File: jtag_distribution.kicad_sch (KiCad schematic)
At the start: 28 parts, among them J16 Conn_ARM_JTAG_SWD_20, SW1 SW_DIP_x04, U2 AMS1117-3.3

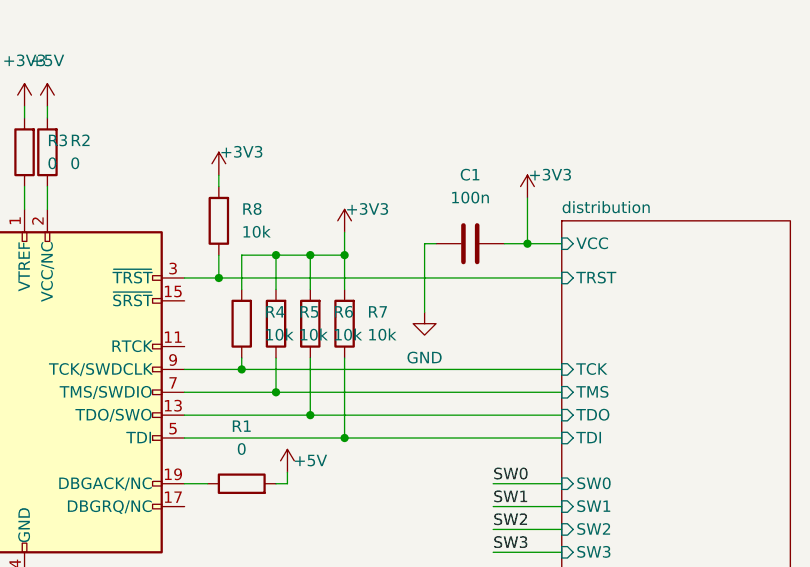
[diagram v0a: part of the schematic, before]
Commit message: change dip switch type, change reset position
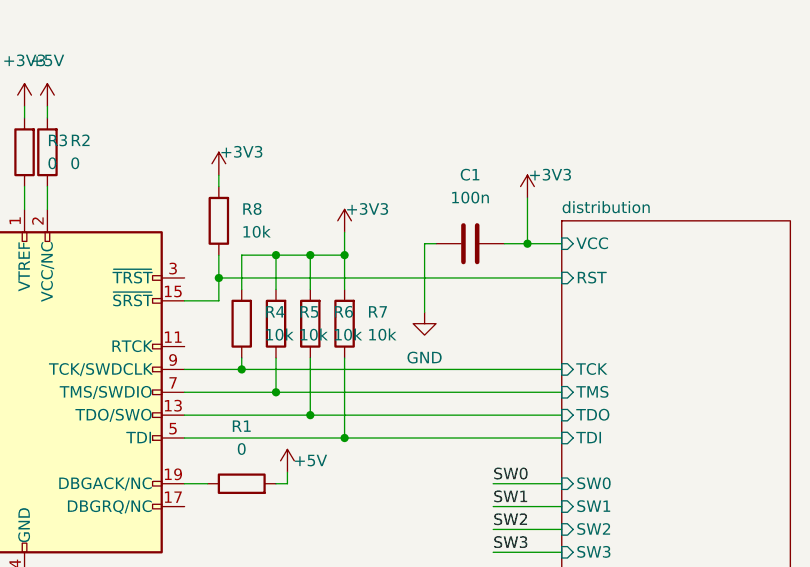
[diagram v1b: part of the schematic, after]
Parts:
- SW1: footprint Button_Switch_SMD:SW_DIP_SPSTx04_Slide_6.7x11.72mm_W8.61mm_P2.54mm_LowProfile -> Button_Switch_THT:SW_DIP_SPSTx04_Slide_6.7x11.72mm_W7.62mm_P2.54mm_LowProfile
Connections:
- net distribution/RST: now reaches J16.15 (~{SRST})
- net distribution/RST: now also R8.1
- net distribution/TRST: no longer names the net of J16.3 (~{TRST})
- net distribution/TRST: no longer R8.1
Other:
- sheet distribution ports: added RST; removed TRST
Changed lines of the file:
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@@
   (junction (at 67.31 157.48) (diameter 0) (color 0 0 0 0)
   )
+  (junction (at 130.81 85.09) (diameter 0) (color 0 0 0 0)
+  )
   (junction (at 212.09 36.83) (diameter 0) (color 0 0 0 0)
   )
@@
   (junction (at 144.78 102.87) (diameter 0) (color 0 0 0 0)
   )
-  (junction (at 130.81 85.09) (diameter 0) (color 0 0 0 0)
-  )
   (junction (at 64.77 154.94) (diameter 0) (color 0 0 0 0)
   )
@@
     (stroke (width 0) (type default))
   )
+  (wire (pts (xy 130.81 85.09) (xy 130.81 87.63))
+    (stroke (width 0) (type default))
+  )
   (wire (pts (xy 137.16 82.55) (xy 137.16 86.36))
     (stroke (width 0) (type default))
@@
     (stroke (width 0) (type default))
   )
-  (wire (pts (xy 127 85.09) (xy 130.81 85.09))
-    (stroke (width 0) (type default))
-  )
   (wire (pts (xy 130.81 85.09) (xy 168.91 85.09))
     (stroke (width 0) (type default))
@@
   )
   (wire (pts (xy 90.17 157.48) (xy 90.17 154.94))
+    (stroke (width 0) (type default))
+  )
+  (wire (pts (xy 127 87.63) (xy 130.81 87.63))
     (stroke (width 0) (type default))
   )
@@
       (effects (font (size 1.27 1.27)))
     )
-    (property "Footprint" "Button_Switch_SMD:SW_DIP_SPSTx04_Slide_6.7x11.72mm_W8.61mm_P2.54mm_LowProfile" (at 80.01 157.48 0)
+    (property "Footprint" "Button_Switch_THT:SW_DIP_SPSTx04_Slide_6.7x11.72mm_W7.62mm_P2.54mm_LowProfile" (at 80.01 157.48 0)
       (effects (font (size 1.27 1.27)) hide)
     )
@@
       (effects (font (size 1.27 1.27)) (justify left))
     )
-    (pin "TRST" input (at 168.91 85.09 180)
-      (effects (font (size 1.27 1.27)) (justify left))
-    )
     (pin "TDI" input (at 168.91 102.87 180)
       (effects (font (size 1.27 1.27)) (justify left))
@@
       (effects (font (size 1.27 1.27)) (justify left))
     )
+    (pin "RST" input (at 168.91 85.09 180)
+      (effects (font (size 1.27 1.27)) (justify left))
+    )
